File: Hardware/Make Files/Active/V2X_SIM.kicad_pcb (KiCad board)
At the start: 2 copper layers, 85 x 56 mm, 50 parts, among them P1 47553-1001, P11 Ficudial2, P13 Ficudial3, P16 Ficudial4, P18 CUR_SEN, P2 SMA, P26 CONN_02X08, P3 SMA, P7 Ficudial1, Q12 IRF9335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

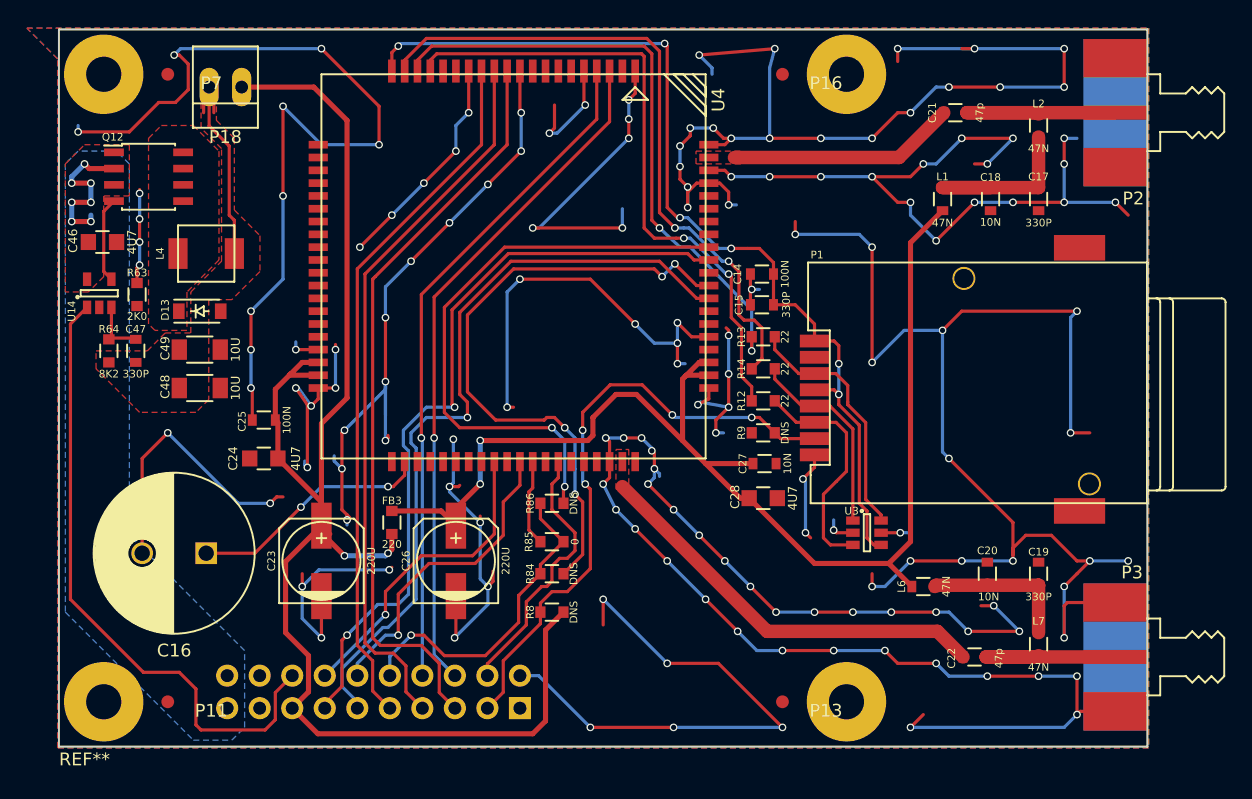
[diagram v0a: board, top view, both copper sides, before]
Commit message: Build pass of main V2X board
ready to verify
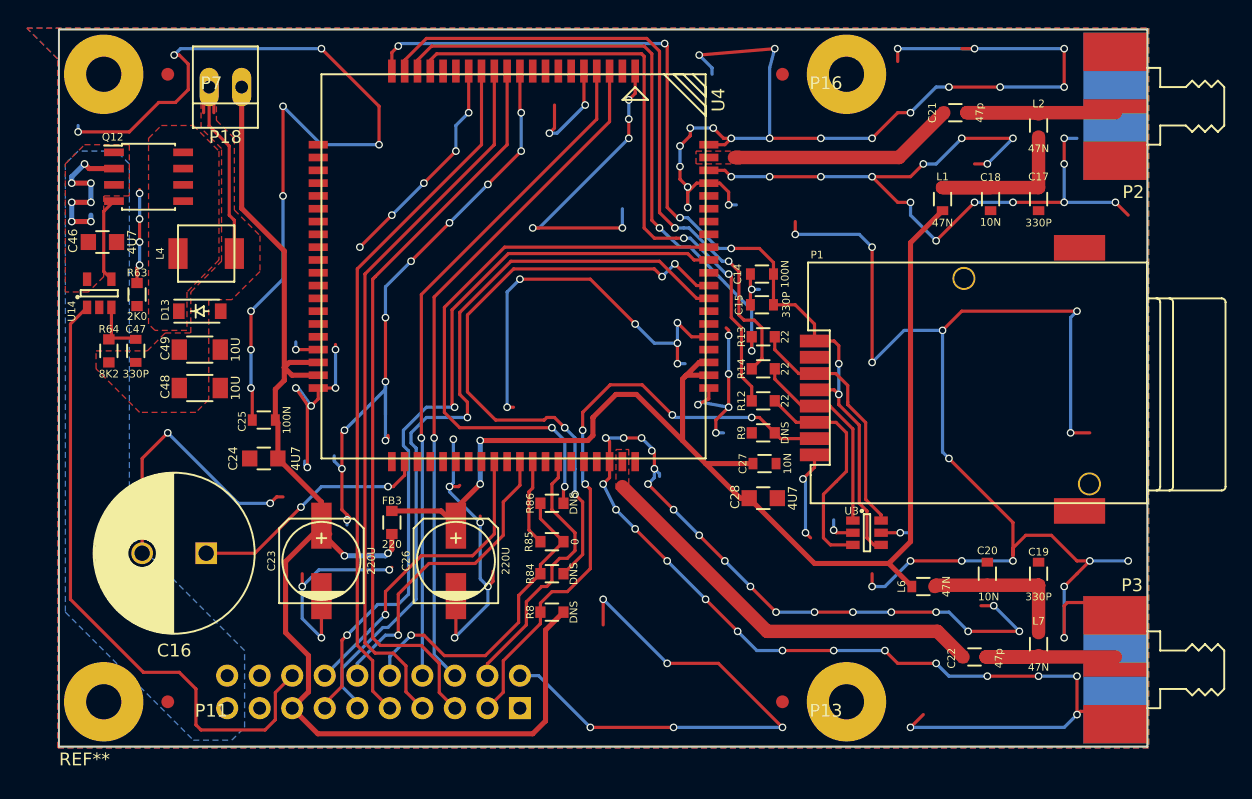
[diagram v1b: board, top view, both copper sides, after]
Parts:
- moved P3 1.00 mm to (198.5, 132.5)
- moved P2 0.50 mm to (198.5, 88.5)
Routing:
- net 4V1_B: track 116.4 -> 99.0 mm
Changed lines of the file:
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@@
   (general
     (links 137)
-    (no_connects 1)
-    (area 101.214287 82.065 206.225 145.700001)
+    (no_connects 2)
+    (area 101.214287 80.375 206.225 148.208333)
     (thickness 1.6)
-    (drawings 6)
-    (tracks 910)
+    (drawings 10)
+    (tracks 909)
     (zones 0)
     (modules 50)
@@
   )
   (module "Custom Parts:SMA-RA_142-0701-801" (layer F.Cu)
-    (at 198.5 131.5 270)
+    (at 198.5 132.5 270)
     (fp_text reference P3 (at -6.6 1.2 360) (layer F.SilkS)
       (effects (font (size 1 1) (thickness 0.15)))
@@
   )
   (module "Custom Parts:SMA-RA_142-0701-801" (layer F.Cu)
-    (at 198.5 89 270)
+    (at 198.5 88.5 270)
     (fp_text reference P2 (at 6.7 1.1 360) (layer F.SilkS)
       (effects (font (size 1 1) (thickness 0.15)))
@@
     (pad "" thru_hole circle (at 58 -49) (size 6.2 6.2) (drill 2.75) (layers *.Cu *.Mask F.SilkS))
     (pad "" thru_hole circle (at 58 0) (size 6.2 6.2) (drill 2.75) (layers *.Cu *.Mask F.SilkS))
+  )
+  (dimension 6 (width 0.3) (layer Cmts.User)
+    (gr_text "6.000 mm" (at 215.35 85.5 90) (layer Cmts.User)
+      (effects (font (size 1.5 1.5) (thickness 0.3)))
+    )
+    (feature1 (pts (xy 198.5 82.5) (xy 216.7 82.5)))
+    (feature2 (pts (xy 198.5 88.5) (xy 216.7 88.5)))
+    (crossbar (pts (xy 214 88.5) (xy 214 82.5)))
+    (arrow1a (pts (xy 214 82.5) (xy 214.586421 83.626504)))
+    (arrow1b (pts (xy 214 82.5) (xy 213.413579 83.626504)))
+    (arrow2a (pts (xy 214 88.5) (xy 214.586421 87.373496)))
+    (arrow2b (pts (xy 214 88.5) (xy 213.413579 87.373496)))
+  )
+  (dimension 6 (width 0.3) (layer Cmts.User)
+    (gr_text "6.000 mm" (at 215.35 135.5 90) (layer Cmts.User)
+      (effects (font (size 1.5 1.5) (thickness 0.3)))
+    )
+    (feature1 (pts (xy 198.5 132.5) (xy 216.7 132.5)))
+    (feature2 (pts (xy 198.5 138.5) (xy 216.7 138.5)))
+    (crossbar (pts (xy 214 138.5) (xy 214 132.5)))
+    (arrow1a (pts (xy 214 132.5) (xy 214.586421 133.626504)))
+    (arrow1b (pts (xy 214 132.5) (xy 213.413579 133.626504)))
+    (arrow2a (pts (xy 214 138.5) (xy 214.586421 137.373496)))
+    (arrow2b (pts (xy 214 138.5) (xy 213.413579 137.373496)))
+  )
+  (dimension 44 (width 0.3) (layer Cmts.User)
+    (gr_text "44.000 mm" (at 215.35 110.5 90) (layer Cmts.User)
+      (effects (font (size 1.5 1.5) (thickness 0.3)))
+    )
+    (feature1 (pts (xy 204.5 88.5) (xy 216.7 88.5)))
+    (feature2 (pts (xy 204.5 132.5) (xy 216.7 132.5)))
+    (crossbar (pts (xy 214 132.5) (xy 214 88.5)))
+    (arrow1a (pts (xy 214 88.5) (xy 214.586421 89.626504)))
+    (arrow1b (pts (xy 214 88.5) (xy 213.413579 89.626504)))
+    (arrow2a (pts (xy 214 132.5) (xy 214.586421 131.373496)))
+    (arrow2b (pts (xy 214 132.5) (xy 213.413579 131.373496)))
+  )
+  (dimension 32 (width 0.3) (layer Cmts.User)
+    (gr_text "32.000 mm" (at 210.35 110.5 90) (layer Cmts.User)
+      (effects (font (size 1.5 1.5) (thickness 0.3)))
+    )
+    (feature1 (pts (xy 198.5 94.5) (xy 211.7 94.5)))
+    (feature2 (pts (xy 198.5 126.5) (xy 211.7 126.5)))
+    (crossbar (pts (xy 209 126.5) (xy 209 94.5)))
+    (arrow1a (pts (xy 209 94.5) (xy 209.586421 95.626504)))
+    (arrow1b (pts (xy 209 94.5) (xy 208.413579 95.626504)))
+    (arrow2a (pts (xy 209 126.5) (xy 209.586421 125.373496)))
+    (arrow2b (pts (xy 209 126.5) (xy 208.413579 125.373496)))
   )
   (gr_line (start 113.5 138.5) (end 113.5 82.5) (angle 90) (layer Edge.Cuts) (width 0.1))
@@
   (segment (start 190 129.6) (end 190 125.9) (width 1.05) (layer F.Cu) (net 22))
   (segment (start 190 125.9) (end 189.9 126) (width 1.05) (layer F.Cu) (net 22))
+  (segment (start 133.75 108.5) (end 131.5 108.5) (width 0.4) (layer F.Cu) (net 23))
+  (segment (start 131.5 108.5) (end 131.1 108.9) (width 0.4) (layer F.Cu) (net 23))
+  (segment (start 133.75 109.5) (end 131.7 109.5) (width 0.4) (layer F.Cu) (net 23))
+  (segment (start 131.7 109.5) (end 131.1 108.9) (width 0.4) (layer F.Cu) (net 23))
+  (segment (start 127.77 87) (end 127.77 96.47) (width 0.4) (layer F.Cu) (net 23))
+  (segment (start 131.1 99.8) (end 131.1 108.9) (width 0.4) (layer F.Cu) (net 23))
+  (segment (start 131.1 108.9) (end 131.1 109.9) (width 0.4) (layer F.Cu) (net 23))
+  (segment (start 127.77 96.47) (end 131.1 99.8) (width 0.4) (layer F.Cu) (net 23))
   (segment (start 152.9 128) (end 151.5 129.4) (width 0.4) (layer F.Cu) (net 23))
   (segment (start 133.72 137.5) (end 131.72 135.5) (width 0.4) (layer F.Cu) (net 23))
@@
   (segment (start 139.5 123.1) (end 139.2 123.4) (width 0.4) (layer F.Cu) (net 23))
   (segment (start 134 121.8) (end 134 121.24918) (width 0.4) (layer F.Cu) (net 23))
-  (segment (start 134 121.24918) (end 134 113.274998) (width 0.4) (layer F.Cu) (net 23))
-  (segment (start 134 113.274998) (end 136 111.274998) (width 0.4) (layer F.Cu) (net 23))
   (segment (start 134 121.24918) (end 131.2 124.04918) (width 0.4) (layer F.Cu) (net 23))
   (segment (start 131.2 124.04918) (end 131.2 129.6) (width 0.4) (layer F.Cu) (net 23))
@@
   (segment (start 132.99 134.23) (end 131.72 135.5) (width 0.4) (layer F.Cu) (net 23))
   (segment (start 134 121.24918) (end 134.65082 121.9) (width 0.4) (layer F.Cu) (net 23))
-  (segment (start 133.75 109.5) (end 131.5 109.5) (width 0.4) (layer F.Cu) (net 23))
-  (segment (start 131.5 109.5) (end 131.6 109.4) (width 0.4) (layer F.Cu) (net 23))
   (segment (start 130.4 113) (end 130.4 110.6) (width 0.4) (layer F.Cu) (net 23))
-  (segment (start 130.4 110.6) (end 131.6 109.4) (width 0.4) (layer F.Cu) (net 23))
-  (segment (start 131.6 109.4) (end 132.5 108.5) (width 0.4) (layer F.Cu) (net 23))
-  (segment (start 132.5 108.5) (end 133.75 108.5) (width 0.4) (layer F.Cu) (net 23))
+  (segment (start 130.4 110.6) (end 131.1 109.9) (width 0.4) (layer F.Cu) (net 23))
   (segment (start 130.6 116) (end 130.6 113.2) (width 0.4) (layer F.Cu) (net 23))
   (segment (start 130.6 113.2) (end 130.4 113) (width 0.4) (layer F.Cu) (net 23))
   (segment (start 134 121.24918) (end 134 119.4) (width 0.4) (layer F.Cu) (net 23))
   (segment (start 134 119.4) (end 130.6 116) (width 0.4) (layer F.Cu) (net 23))
-  (segment (start 127.77 87) (end 133.4 87) (width 0.4) (layer F.Cu) (net 23))
-  (segment (start 133.4 87) (end 136 89.6) (width 0.4) (layer F.Cu) (net 23))
-  (segment (start 136 89.6) (end 136 111.274998) (width 0.4) (layer F.Cu) (net 23))
   (via (at 116 97.5) (size 0.6) (drill 0.4) (layers F.Cu B.Cu) (net 24))
   (segment (start 116 97.5) (end 116 97) (width 0.4) (layer B.Cu) (net 24))

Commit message: V1.2 pass complete and ready to order
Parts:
- 4V1 CUR SEN: renamed from P18
- moved 4V1 CUR SEN 21.9 mm to (117.0, 106.8), turned to 270 degrees
- moved C16 21.7 mm to (128.5, 102.0)
- moved R64 19.0 mm to (119.0, 126.5)
- moved C47 19.0 mm to (121.0, 126.5)
- moved R63 18.9 mm to (121.0, 122.0)
- moved C46 18.7 mm to (118.3, 117.7)
- moved Q12 18.6 mm to (122.5, 112.5)
- moved U14 18.4 mm to (118.0, 121.5)
- moved C48 18.0 mm to (125.0, 128.5), turned to 180 degrees
- moved C49 18.0 mm to (125.0, 125.5), turned to 180 degrees
- moved D13 18.0 mm to (125.0, 122.5), turned to 180 degrees
- moved L4 18.0 mm to (125.5, 118.0)
- moved C25 4.74 mm to (131.0, 108.5), turned to 90 degrees
- moved C24 2.50 mm to (132.0, 116.0), turned to 270 degrees
- moved C22 1.00 mm to (185.0, 132.5)
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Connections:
- REF** pad : (no net) -> GND
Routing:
- net GND: track 715.5 -> 839.4 mm, vias 157 -> 194
- net 4V1F1: track 97.4 -> 26.9 mm
- net 4V1_B: track 99.0 -> 59.3 mm
- net 4V1_EN_B: track 49.5 -> 27.7 mm
- net Net-(C47-Pad1): track 18.1 -> 0.00 mm
- net SIMCARD_B: track 48.1 -> 57.5 mm
- net Net-(C16-Pad1): track 19.9 -> 26.7 mm, vias 2 -> 1
- net SIM_RI: track 49.8 -> 46.0 mm
- net Net-(C47-Pad2): track 4.87 -> 7.19 mm
- net PC_WAKE: track 6.75 -> 8.74 mm
- net SIM_RF_OFF_B: track 21.1 -> 23.0 mm, vias 0 -> 2
- net SIM_DTR: track 46.0 -> 44.3 mm
- net Net-(C19-Pad2): track 12.0 -> 12.9 mm
- net Net-(C17-Pad2): track 15.2 -> 15.7 mm
- added copper zone on F.Cu, net 4V1F1
- added copper zone on F.Cu, net 4V1_B
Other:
- board text added: "GPS SILVER"
- board text added: "GSM GOLD"
- board text added: "JAGUAR LAND ROVER OSTC RVI V2X V1.2 2015 M2M+GPS BOARD"
- board text added: "Jesse Banks"
